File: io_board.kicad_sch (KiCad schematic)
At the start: 20 parts, among them J1 TBP02R1-381-04, J10 TBP02R1-381-02, J11 TBP02R1-381-02, J12 TBP02R1-381-04, J13 CI1103M1VR0, J15 TBP02R1-381-02, J2 25SH-B-03-TR, J3 TBP02R1-381-02, J4 TBP02R1-381-02, J5 TBP02R1-381-02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

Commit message: added a reset button for the rp2040
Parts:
- added SW1: SW_Push, symbol Switch:SW_Push
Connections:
- net GND: now also SW1.1
- net RESET: now reaches U2.30 (RUN)
- net RESET: now also SW1.2
- no-connect marks 7 -> 6
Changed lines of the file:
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@@
   (no_connect (at 246.38 64.77))
   (no_connect (at 246.38 57.15))
-  (no_connect (at 246.38 82.55))
   (wire (pts (xy 246.38 87.63) (xy 262.89 87.63))
     (stroke (width 0) (type default))
@@
     (stroke (width 0) (type default))
   )
+  (wire (pts (xy 201.93 34.29) (xy 204.47 34.29))
+    (stroke (width 0) (type default))
+  )
   (wire (pts (xy 113.03 146.05) (xy 93.98 146.05))
     (stroke (width 0) (type default))
@@
     (stroke (width 0) (type default))
   )
+  (wire (pts (xy 204.47 34.29) (xy 204.47 36.83))
+    (stroke (width 0) (type default))
+  )
   (wire (pts (xy 27.94 175.26) (xy 41.91 175.26))
     (stroke (width 0) (type default))
@@
     (stroke (width 0) (type default))
   )
+  (wire (pts (xy 246.38 82.55) (xy 260.35 82.55))
+    (stroke (width 0) (type default))
+  )
   (wire (pts (xy 210.82 67.31) (xy 196.85 67.31))
     (stroke (width 0) (type default))
@@
     (stroke (width 0) (type default))
   )
+  (wire (pts (xy 191.77 34.29) (xy 182.88 34.29))
+    (stroke (width 0) (type default))
+  )
   (wire (pts (xy 236.22 30.48) (xy 245.11 30.48))
     (stroke (width 0) (type default))
@@
     (effects (font (size 1.27 1.27)) (justify right bottom))
   )
+  (label "RESET" (at 182.88 34.29 0) (fields_autoplaced)
+    (effects (font (size 1.27 1.27)) (justify left bottom))
+  )
   (label "INVERTER_RX" (at 97.79 148.59 0) (fields_autoplaced)
     (effects (font (size 1.27 1.27)) (justify left bottom))
@@
   )
   (label "LED0_CAT" (at 152.4 111.76 180) (fields_autoplaced)
+    (effects (font (size 1.27 1.27)) (justify right bottom))
+  )
+  (label "RESET" (at 260.35 82.55 180) (fields_autoplaced)
     (effects (font (size 1.27 1.27)) (justify right bottom))
   )
@@
         (path "/93c7735d-4528-42c1-a290-28f8c7f58a04"
           (reference "J5") (unit 1)
+        )
+      )
+    )
+  )
+  (symbol (lib_id "power:GND") (at 204.47 36.83 0) (mirror y) (unit 1)
+    (in_bom yes) (on_board yes) (dnp no) (fields_autoplaced)
+    (property "Reference" "#PWR045" (at 204.47 43.18 0)
+      (effects (font (size 1.27 1.27)) hide)
+    )
+    (property "Value" "GND" (at 204.47 40.9631 0)
+      (effects (font (size 1.27 1.27)))
+    )
+    (property "Footprint" "" (at 204.47 36.83 0)
+      (effects (font (size 1.27 1.27)) hide)
+    )
+    (property "Datasheet" "" (at 204.47 36.83 0)
+      (effects (font (size 1.27 1.27)) hide)
+    )
+    (pin "1")
+    (instances
+      (project "io_board"
+        (path "/93c7735d-4528-42c1-a290-28f8c7f58a04"
+          (reference "#PWR045") (unit 1)
         )
       )
@@
         )
       )
+    )
+  )
+  (symbol (lib_id "Switch:SW_Push") (at 196.85 34.29 0) (mirror y) (unit 1)
+    (in_bom yes) (on_board yes) (dnp no) (fields_autoplaced)
+    (property "Reference" "SW1" (at 196.85 27.2247 0)
+      (effects (font (size 1.27 1.27)))
+    )
+    (property "Value" "SW_Push" (at 196.85 29.6489 0)
+      (effects (font (size 1.27 1.27)))
+    )
+    (property "Footprint" "" (at 196.85 29.21 0)
+      (effects (font (size 1.27 1.27)) hide)
+    )
+    (property "Datasheet" "~" (at 196.85 29.21 0)
+      (effects (font (size 1.27 1.27)) hide)
+    )
+    (pin "1")
+    (pin "2")
+    (instances
+      (project "io_board"
+        (path "/93c7735d-4528-42c1-a290-28f8c7f58a04"
+          (reference "SW1") (unit 1)
+        )
+      )

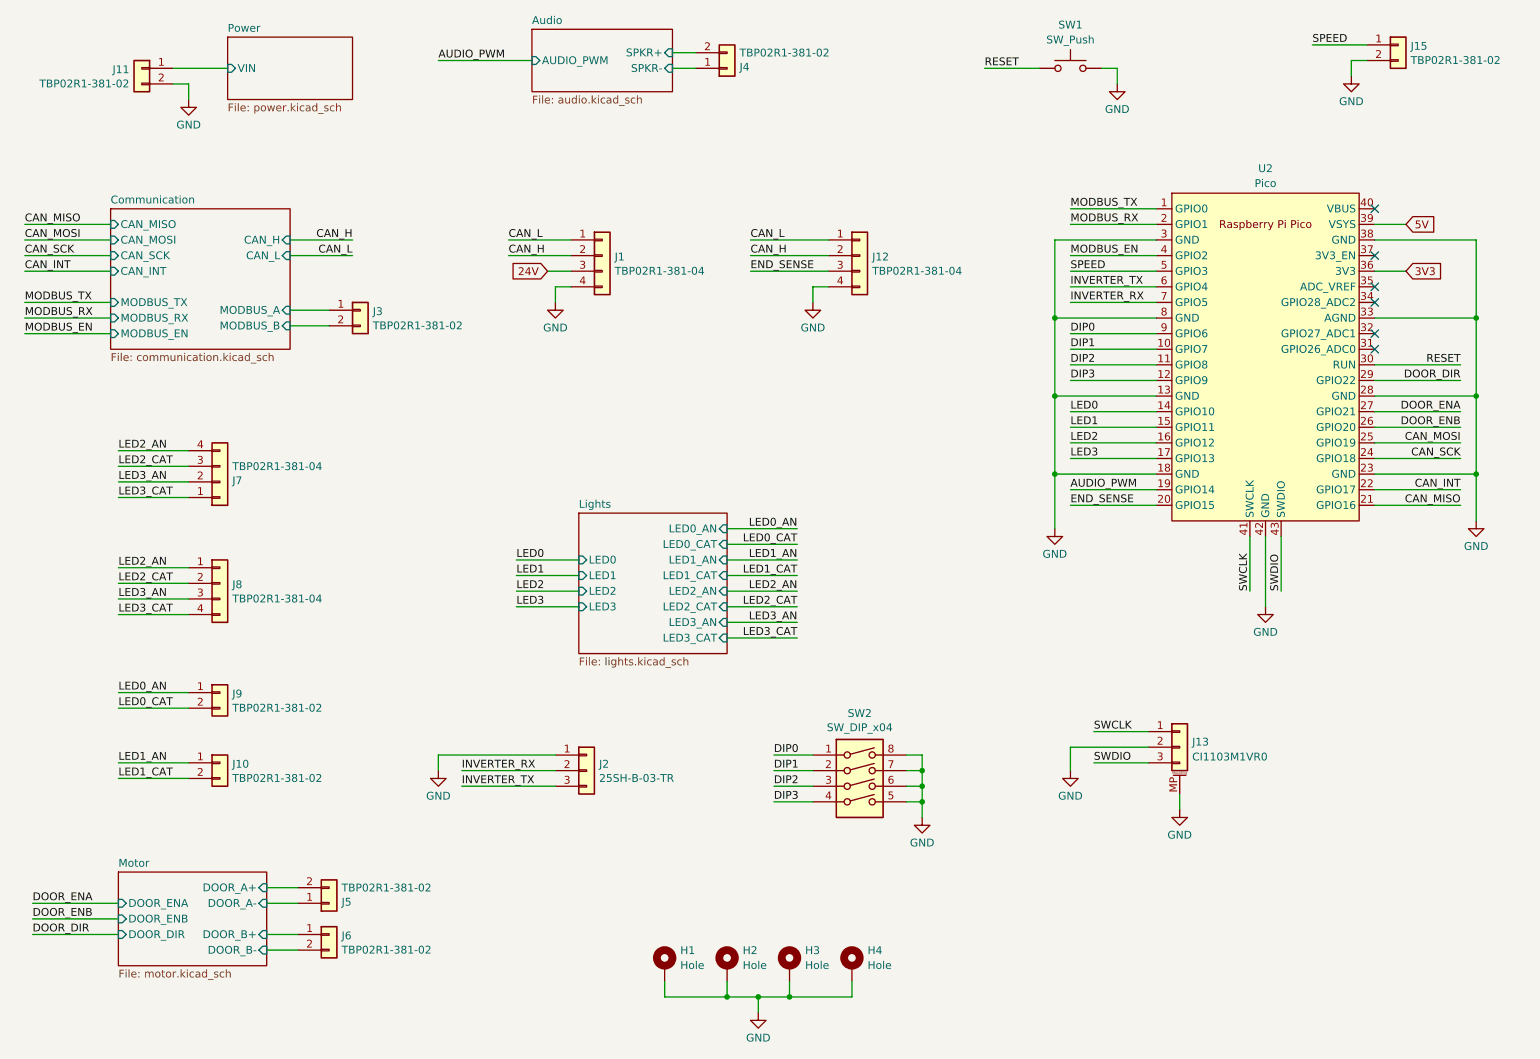
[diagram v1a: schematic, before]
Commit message: removed the mcp2515 can controller because I can use the can2040 library instead
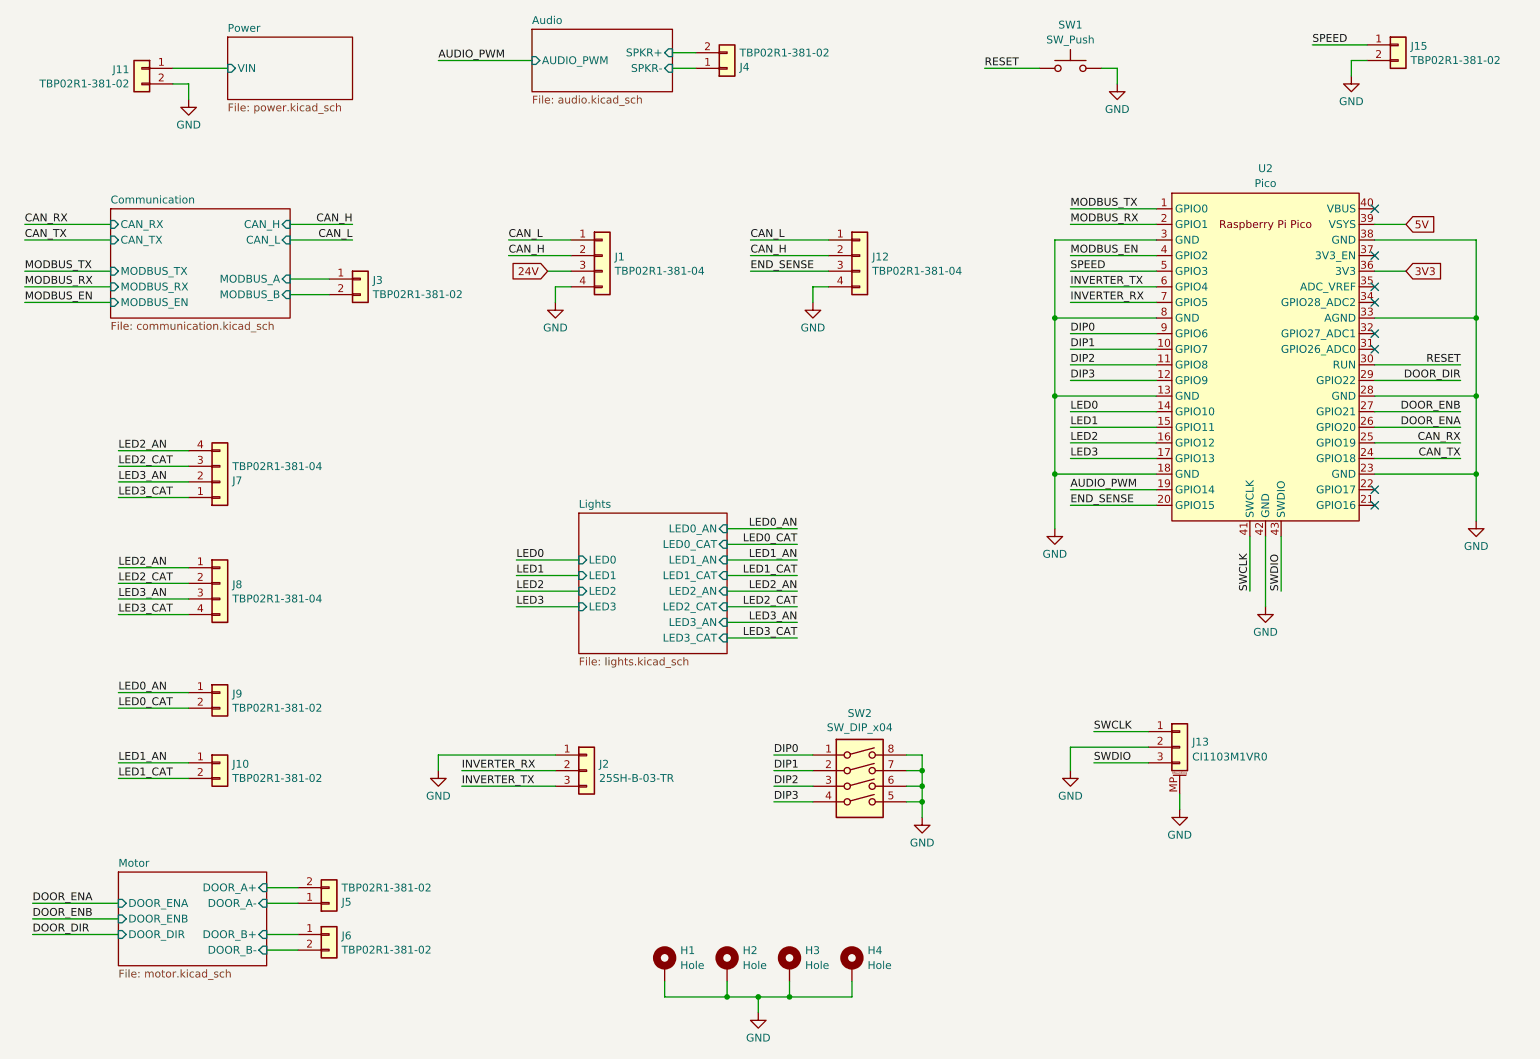
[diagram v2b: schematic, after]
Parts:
- SW1: footprint (none) -> Button_Switch_THT:SW_PUSH_6mm
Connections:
- net DOOR_ENA: now also U2.26 (GPIO20); no longer U2.27 (GPIO21)
- net DOOR_ENB: now also U2.27 (GPIO21); no longer U2.26 (GPIO20)
- net CAN_INT: no longer names the net of U2.22 (GPIO17)
- net CAN_MISO: no longer names the net of U2.21 (GPIO16)
- net CAN_MOSI renamed CAN_RX
- net CAN_SCK renamed CAN_TX
- no-connect marks 6 -> 8
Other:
- sheet Communication ports: added CAN_RX, CAN_TX; removed CAN_INT, CAN_MISO, CAN_MOSI, CAN_SCK
- moved on the sheet: J3
